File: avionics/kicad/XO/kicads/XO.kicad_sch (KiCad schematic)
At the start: 52 parts, among them SW1 SW_DIP_x02, X2Y-CAN 4.7nF_X2Y, X2Y-RS485 4.7nF_X2Y

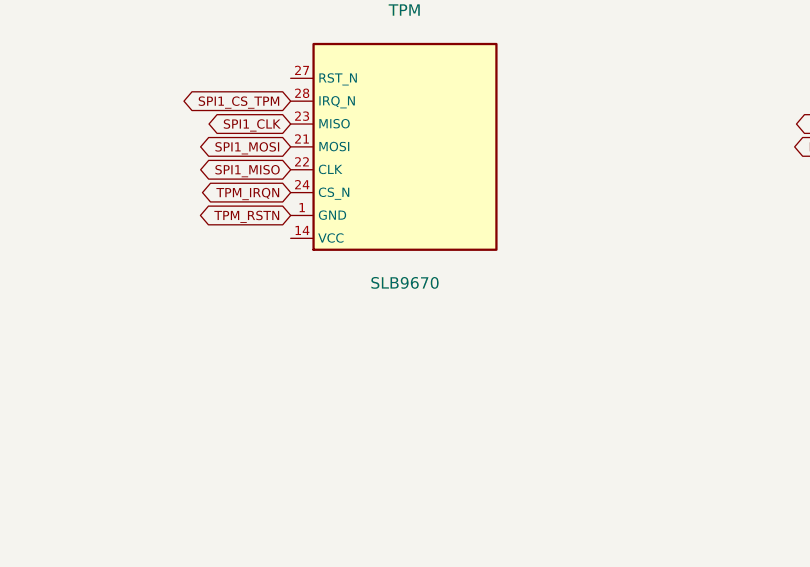
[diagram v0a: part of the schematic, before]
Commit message: Migrate fleet TPM from Infineon SLB9670 to SLB9672
Replaces every active reference to the SLB9670 TPM with SLB9672 across
KiCad symbols/schematics/PCBs/netlists, generator scripts, firmware
device-tree overlays, and documentation (REFERENCES.md, WBS/TODO,
current-specification, graphical build guide). Archived files, frozen
revision snapshots, and the old datasheet PDF are left untouched.

- Added avionics/datasheets/SLB_9672XU20_Infineon.pdf (Infineon DS Rev
  1.3, 2024-11-18) and a new clean-room symbol/pinmap
  (Observer_SLB9672_TPM.kicad_sym, SLB9672XU2_0_pinmap.csv), replacing
  the superseded SLB9670 symbol/pinmap.
- Verified the physical footprint is unchanged (5x5mm body, 0.5mm
  pitch, 32-pin QFN, 3.6x3.6mm exposed pad per both datasheets), so the
  existing Package_DFN_QFN:QFN-32-1EP_5x5mm_P0.5mm_EP3.45x3.45mm
  footprint was reused as-is. Pin *functions* do differ (SLB9672 makes
  pins 1/14/22 the mandatory VDD pins vs 8/22 on SLB9670; pin 6 is now a
  true no-connect instead of GPIO; pins 3/4/7 are GPIO_00/01/02 instead
  of NCI/NCI/PP) -- the new symbol and every net-map/pinmap that lists
  pin functions reflect the corrected pinout.
- Populated the corrected component into Observer, Commo, Flight
  Engineer, and CAN-PERIPH-GW-1's schematics (lib_symbol block +
  instances) and into every board's PCB Value/property text. Pilot's
  and XO's own independently-authored inline TPM symbols were text-
  renamed only, preserving their pre-existing (and separately tracked)
  wrong-pin-number defect -- out of scope for this swap.
- Firmware: infineon,slb9670 -> infineon,slb9672 compatible string and
  tpm_slb9670: -> tpm_slb9672: node label in both active cape DTS
  overlays.
- REFERENCES.md REF-SENSOR-011 updated in place with validated Infineon
  URLs; new open items logged for (a) re-running kicad-cli ERC/DRC
  (unavailable in this environment) and (b) a newly-found, unrelated
  pre-existing footprint-mismatch defect on XO's placed TPM.
- PROJECT_INDEX.md / t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
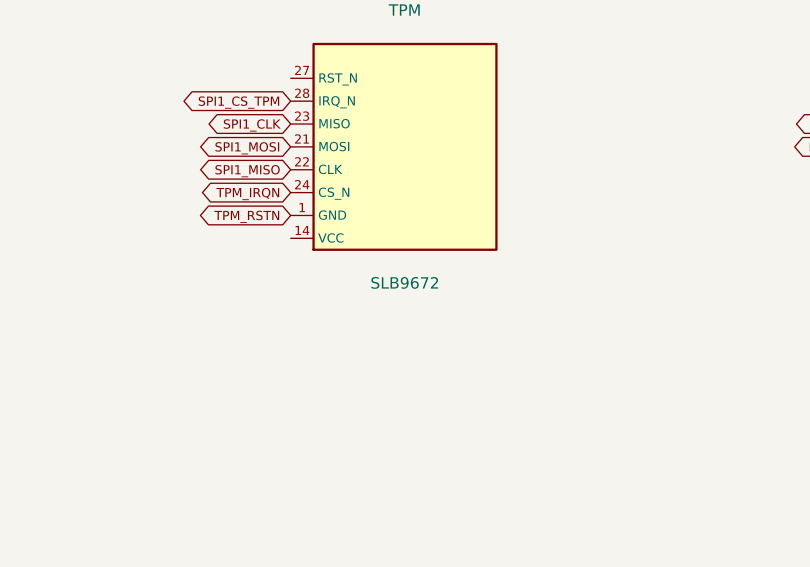
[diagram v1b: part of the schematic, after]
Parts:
- TPM: value SLB9670 -> SLB9672; symbol SLB9670 -> SLB9672
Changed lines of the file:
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@@
     (property "Intersheet References" "${INTERSHEET_REFS}" (at 292.70 352.54 0)
       (effects (font (size 1.016 1.016)) (hide yes))))
-  (symbol (lib_id "SLB9670") (at 210.00 350.00 0)
+  (symbol (lib_id "SLB9672") (at 210.00 350.00 0)
     (unit 1) (exclude_from_sim no) (in_bom yes) (on_board yes) (dnp no)
     (property "Reference" "TPM" (at 210.00 334.84 0) (effects (font (size 1.27 1.27))))
-    (property "Value" "SLB9670" (at 210.00 365.16 0) (effects (font (size 1.27 1.27))))
+    (property "Value" "SLB9672" (at 210.00 365.16 0) (effects (font (size 1.27 1.27))))
     (property "Footprint" "" (at 0 0 0) (effects (font (size 1.27 1.27)) (hide yes)))
     (property "Datasheet" "" (at 0 0 0) (effects (font (size 1.27 1.27)) (hide yes)))

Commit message: feat(avionics): XO schematic-first rebuild to ERC 0; PCB placement in progress
Replaces XO's legacy schematic/PCB (169 sch refs vs 43 PCB footprints, 564
ERC violations) with a fresh generator pipeline matching Pilot's method
(gen_xo_sch.py / gen_xo_footprints.py / gen_xo_pcb.py), all datasheet-verified.

Fleet-shared blocks reused verbatim from Pilot (same parts, same pin tables,
_B_-suffixed nets per XO.md's own documented bus-sharing rationale): ISOW1044
CAN-FD, ISOW1412 RS-485, HI-1573 + PM-DB2791S MIL-STD-1553B (retires the
DS26LV31/32 + fake "SM-1553-11" defect, same fix as Pilot), SLB9672 TPM,
DP83825I Ethernet PHY x1 (single PHY per WBS.md "XO: 1x PHY (RMII0)" —
resolves a 3-way doc contradiction over whether XO has Ethernet in favor of
WBS's more authoritative, more recent "restored at Rev R" entry).

New XO-unique blocks, each pin table transcribed from its own OEM datasheet:
RFD900x SiK UHF radio, RFM95W LoRa module, WL1837MOD WiFi+BT (~14 of 100
balls carry a net this pass, a disclosed scope calibration), TPS63031 RF
buck-boost rail, W25Q128JV SPI NOR flash, ATF16V8BQL used as a logging
write-block interlock (JEDEC fuse map is a firmware deliverable, out of
scope here), three antenna filter/ESD chains, microSD slot.

Two part-number defects found in XO.md's own antenna-filter BOM and
corrected (flagged, not silently fixed): Johanson "0915LP15B0100E" and
"2450BP15B050E" do not exist in Johanson's catalog (confirmed against their
product listings) — substituted with the closest real parts found
(0915LP15B026E, 2450BP15E0100); NEEDS owner confirmation. XO.md's cited
microSD connector "Molex 503182-1852" could not be verified real —
replaced with the confirmed-real Connector_Card:microSD_HC_Molex_104031-0811
already in KiCad's system library. RCLAMP0502B's datasheet PDF could not be
obtained from any source tried; its footprint is a reasonable SOD-882
estimate, not pixel-verified — flagged for a real datasheet fetch.

ERC 0 confirmed (kicad-cli sch erc --sev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
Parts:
- removed 1553-DRV: DS26LV31, symbol DS26LV31
- removed 1553-RCV: DS26LV32, symbol DS26LV32
- removed 1553-XFM: SM-1553-11, symbol SM-1553-11
- removed CAN-TR: ISOW1044BDFMR, Package_SO:SOIC-20W_7.5x12.8mm_P1.27mm, symbol ISOW1044BDFMR
- removed CMC-CAN, CMC-RS485, CM_ETH_B: SRF2012-100Y, Inductor_SMD:L_0805_2012Metric, symbol SRF2012
- removed D_1553: SMAJ33CA, Diode_SMD:D_SMA, symbol SMAJ33CA
- removed D_ANT_LORA, D_ANT_SIK, D_ANT_WIFI: RCLAMP0502B, Diode_SMD:D_SOD-882, symbol RCLAMP0502B
- removed D_CAN, D_RS485, D_XCVR_TVS, TVS_ETHB_RX, TVS_ETHB_TX: PRTR5V0U2X, Package_TO_SOT_SMD:SOT-363_SC-70-6, symbol PRTR5V0U2X
- removed ETH-PHY: DP83825I, Package_QFP:LQFP-32_7x7mm_P0.8mm, symbol DP83825I
- removed FB_PWR: 742792512, Inductor_SMD:L_0805_2012Metric, symbol Ferrite_Bead
- removed FL_LORA, FL_SIK: 0915LP15B0100E, Filter:BPF_1206, symbol BPF_915
- removed FL_WIFI: 2450BP15B050E, Filter:BPF_1206, symbol BPF_2400
- removed HX1188_B: HX1188NL, Package_SO:SOIC-16_3.9x9.9mm_P1.27mm, symbol HX1188NL
- removed J_1553: SM04B-GHS-TB-1MP — MIL-STD-1553B, Connector_JST:JST_GH_SM04B-GHS-TB_1x04-1MP_P1.25mm_Horizontal, symbol Conn_JST_GH_04P
- removed J_485: SM03B-GHS-TB-1MP — RS-485, Connector_JST:JST_GH_SM03B-GHS-TB_1x03-1MP_P1.25mm_Horizontal, symbol Conn_JST_GH_03P
- removed J_CAN: SM03B-GHS-TB-1MP — CAN FD, Connector_JST:JST_GH_SM03B-GHS-TB_1x03-1MP_P1.25mm_Horizontal, symbol Conn_JST_GH_03P
- removed J_ETH_B: SM06B-GHS-TB-1MP, Connector_JST:JST_GH_SM06B-GHS-TB_1x06-1MP_P1.25mm_Horizontal, symbol Conn_JST_GH_06P
- removed J_PWR: JST_GH_04P — Power Input, Connector_JST:JST_GH_SM04B-GHS-TB_1x04-1MP_P1.25mm_Horizontal, symbol Conn_JST_GH_04P
- removed J_SD: microSD, symbol MicroSD
- removed J_SIK_ANT: U.FL-R-SMT-1, Connector_Coaxial:U.FL_Hirose_UFL-R-SMT-1_Vertical, symbol Conn_UFL
- removed J_SMA_LORA, J_SMA_SIK, J_SMA_WIFI: Conn_SMA, Connector_Coaxial:SMA_Vertical_Straight, symbol Conn_SMA
- removed J_XCVR: Conn_JST_GH_06P, Connector_JST:JST_GH_SM06B-GHS-TB_1x06-1MP_P1.25mm_Horizontal, symbol Conn_JST_GH_06P
- removed LOAD-ADC: HX711, symbol HX711
- removed LORA: RFM95W, symbol RFM95W
- removed NOR-FLASH: W25Q128JV, symbol W25Q128JV
- removed PB2-P1: PB2I-P1-2x18, symbol Conn_36
- removed PB2-P2: PB2I-P2-2x18, symbol Conn_36
- removed PWM-I2C: PCA9685, symbol PCA9685
- removed RS485: ISOW1412, Package_SO:SOIC-20W_7.5x12.8mm_P1.27mm, symbol ISOW1412
- removed R_RBIAS_B: 49.9R_1%, Resistor_SMD:R_0402_1005Metric, symbol R_SMD
- removed R_SBUS_RX, R_XCVR_RX: 100R, Resistor_SMD:R_0402_1005Metric, symbol R_SMD
- removed SD-WB: ATF16V8BQL, symbol ATF16V8BQL
- removed SW1: SW_DIP_x02, Package_DIP:DIP-4_W7.62mm, symbol SW_DIP_x02
- removed TPM: SLB9672, symbol SLB9672
- removed U_ETH_B_1V8: TPS62933, Package_SO:SOIC-8_3.9x4.9mm_P1.27mm, symbol TPS62933
- removed U_SBUS_B: 74LVC1G14GW, Package_TO_SOT_SMD:SOT-23-5, symbol 74LVC1G14
- removed WIFI & BT: WL1837MOD, symbol WL1837MOD
- removed WINCH DRV: DRV8833, symbol DRV8833
- removed X2Y-CAN, X2Y-RS485: 4.7nF_X2Y, Capacitor_SMD:C_0402_1005Metric, symbol X2Y_4N7
- added 1553-XCVR: HI-1573PCI, Package_DFN_QFN:QFN-44-1EP_7x7mm_P0.5mm_EP5.2x5.2mm, symbol XO:S_1553-XCVR
- added 1553-XFM: PM-DB2791S, Serenity-Custom:Xfmr_1553_SMD_0.40in_8pin, symbol XO:S_1553-XFM
- added C-1553A: 100nF, Capacitor_SMD:C_0402_1005Metric, symbol XO:S_C-1553A
- added C-1553B: 100nF, Capacitor_SMD:C_0402_1005Metric, symbol XO:S_C-1553B
- added C-1553C: 10uF 6.3V X5R, Capacitor_SMD:C_0805_2012Metric, symbol XO:S_C-1553C
- added C-1V8-IN: 1uF, Capacitor_SMD:C_0402_1005Metric, symbol XO:S_C-1V8-IN
- added C-1V8-OUT: 1uF, Capacitor_SMD:C_0402_1005Metric, symbol XO:S_C-1V8-OUT
- added C-25M: 100nF, Capacitor_SMD:C_0402_1005Metric, symbol XO:S_C-25M
- added C-3V3-HF: 100nF, Capacitor_SMD:C_0402_1005Metric, symbol XO:S_C-3V3-HF
- added C-3V3-IN: 10uF 10V X5R, Capacitor_SMD:C_0805_2012Metric, symbol XO:S_C-3V3-IN
- added C-3V3-O1: 22uF 6.3V X5R, Capacitor_SMD:C_0805_2012Metric, symbol XO:S_C-3V3-O1
- added C-3V3-O2: 22uF 6.3V X5R, Capacitor_SMD:C_0805_2012Metric, symbol XO:S_C-3V3-O2
- added C-485-1: 10nF, Capacitor_SMD:C_0201_0603Metric, symbol XO:S_C-485-1
- added C-485-2: 10uF 10V X5R, Capacitor_SMD:C_0805_2012Metric, symbol XO:S_C-485-2
- added C-485-3: 100nF, Capacitor_SMD:C_0402_1005Metric, symbol XO:S_C-485-3
- added C-485-4: 10nF, Capacitor_SMD:C_0201_0603Metric, symbol XO:S_C-485-4
- added C-485-5: 10uF 10V X5R, Capacitor_SMD:C_0805_2012Metric, symbol XO:S_C-485-5
- added C-485-6: 100nF, Capacitor_SMD:C_0402_1005Metric, symbol XO:S_C-485-6
- added C-BS: 10nF 2kV, Capacitor_SMD:C_1808_4520Metric, symbol XO:S_C-BS
- added C-BST: 100nF, Capacitor_SMD:C_0402_1005Metric, symbol XO:S_C-BST
- added C-CAN1: 10nF, Capacitor_SMD:C_0201_0603Metric, symbol XO:S_C-CAN1
- added C-CAN2: 10uF 10V X5R, Capacitor_SMD:C_0805_2012Metric, symbol XO:S_C-CAN2
- added C-CAN3: 100nF, Capacitor_SMD:C_0402_1005Metric, symbol XO:S_C-CAN3
- added C-CAN4: 10nF, Capacitor_SMD:C_0201_0603Metric, symbol XO:S_C-CAN4
- added C-CAN5: 10uF 10V X5R, Capacitor_SMD:C_0805_2012Metric, symbol XO:S_C-CAN5
- added C-CAN6: 100nF, Capacitor_SMD:C_0402_1005Metric, symbol XO:S_C-CAN6
- added C-FLASH1: 100nF, Capacitor_SMD:C_0402_1005Metric, symbol XO:S_C-FLASH1
- added C-IN1: 47uF 10V X5R, Capacitor_SMD:C_1210_3225Metric, symbol XO:S_C-IN1
- added C-IN2: 10uF 10V X5R, Capacitor_SMD:C_0805_2012Metric, symbol XO:S_C-IN2
- added C-IN3: 100nF, Capacitor_SMD:C_0402_1005Metric, symbol XO:S_C-IN3
- added C-LORA1: 100nF, Capacitor_SMD:C_0402_1005Metric, symbol XO:S_C-LORA1
- added C-PHY-A1: 10nF, Capacitor_SMD:C_0201_0603Metric, symbol XO:S_C-PHY-A1
- added C-PHY-A2: 100nF, Capacitor_SMD:C_0402_1005Metric, symbol XO:S_C-PHY-A2
- added C-PHY-A3: 1uF, Capacitor_SMD:C_0402_1005Metric, symbol XO:S_C-PHY-A3
- added C-PHY-CRD1: 100nF, Capacitor_SMD:C_0402_1005Metric, symbol XO:S_C-PHY-CRD1
- added C-PHY-CRD2: 1uF, Capacitor_SMD:C_0402_1005Metric, symbol XO:S_C-PHY-CRD2
- added C-PHY-CTD1: 100nF, Capacitor_SMD:C_0402_1005Metric, symbol XO:S_C-PHY-CTD1
- added C-PHY-CTD2: 1uF, Capacitor_SMD:C_0402_1005Metric, symbol XO:S_C-PHY-CTD2
- added C-PLD1: 100nF, Capacitor_SMD:C_0402_1005Metric, symbol XO:S_C-PLD1
- added C-RF-IN1: 10uF 10V X5R, Capacitor_SMD:C_0805_2012Metric, symbol XO:S_C-RF-IN1
- added C-RF-IN2: 100nF, Capacitor_SMD:C_0402_1005Metric, symbol XO:S_C-RF-IN2
- added C-RF-O1: 22uF 6.3V X5R, Capacitor_SMD:C_0805_2012Metric, symbol XO:S_C-RF-O1
- added C-RF-O2: 22uF 6.3V X5R, Capacitor_SMD:C_0805_2012Metric, symbol XO:S_C-RF-O2
- added C-SIK1: 10uF 10V X5R, Capacitor_SMD:C_0805_2012Metric, symbol XO:S_C-SIK1
- added C-SIK2: 100nF, Capacitor_SMD:C_0402_1005Metric, symbol XO:S_C-SIK2
- added C-SS: 10nF, Capacitor_SMD:C_0201_0603Metric, symbol XO:S_C-SS
- added C-TPM1: 1uF, Capacitor_SMD:C_0402_1005Metric, symbol XO:S_C-TPM1
- added C-TPM2: 100nF, Capacitor_SMD:C_0402_1005Metric, symbol XO:S_C-TPM2
- added C-TPM3: 100nF, Capacitor_SMD:C_0402_1005Metric, symbol XO:S_C-TPM3
- added C-TPM4: 100nF, Capacitor_SMD:C_0402_1005Metric, symbol XO:S_C-TPM4
- added C-WIFI1: 100nF, Capacitor_SMD:C_0402_1005Metric, symbol XO:S_C-WIFI1
- added C-WIFI2: 10uF 6.3V X5R, Capacitor_SMD:C_0805_2012Metric, symbol XO:S_C-WIFI2
- added CAN-TR: ISOW1044BDFMR, Package_SO:SOIC-20W_7.5x12.8mm_P1.27mm, symbol XO:S_CAN-TR
- added CMC-CAN: SRF2012-100Y, Serenity-Custom:Bourns_SRF2012_4T, symbol XO:S_CMC-CAN
- added CMC-RS485: SRF2012-100Y, Serenity-Custom:Bourns_SRF2012_4T, symbol XO:S_CMC-RS485
- added D-ANT-LORA: RCLAMP0502B, Serenity-Custom:RCLAMP0502B_SOD882, symbol XO:S_D-ANT-LORA
- added D-ANT-SIK: RCLAMP0502B, Serenity-Custom:RCLAMP0502B_SOD882, symbol XO:S_D-ANT-SIK
- added D-ANT-WIFI: RCLAMP0502B, Serenity-Custom:RCLAMP0502B_SOD882, symbol XO:S_D-ANT-WIFI
- added ETH-PHY: DP83825IRHBR, Package_DFN_QFN:Texas_RMQ0024A_WQFN-24-1EP_3x3mm_P0.4mm_EP1.9x1.9mm, symbol XO:S_ETH-PHY
- added FB-SDIO1: 742792510, Inductor_SMD:L_0805_2012Metric, symbol XO:S_FB-SDIO1
- added FB-SDIO2: 742792510, Inductor_SMD:L_0805_2012Metric, symbol XO:S_FB-SDIO2
- added FB-SDIO3: 742792510, Inductor_SMD:L_0805_2012Metric, symbol XO:S_FB-SDIO3
- added FB-SDIO4: 742792510, Inductor_SMD:L_0805_2012Metric, symbol XO:S_FB-SDIO4
- added FB-SDIO5: 742792510, Inductor_SMD:L_0805_2012Metric, symbol XO:S_FB-SDIO5
- added FB-SDIO6: 742792510, Inductor_SMD:L_0805_2012Metric, symbol XO:S_FB-SDIO6
- added FB-SIK1: 742792510, Inductor_SMD:L_0805_2012Metric, symbol XO:S_FB-SIK1
- added FB-SIK2: 742792510, Inductor_SMD:L_0805_2012Metric, symbol XO:S_FB-SIK2
- added FB-SIK3: 742792510, Inductor_SMD:L_0805_2012Metric, symbol XO:S_FB-SIK3
- added FB-SIK4: 742792510, Inductor_SMD:L_0805_2012Metric, symbol XO:S_FB-SIK4
- added FB1: 742792510, Inductor_SMD:L_0805_2012Metric, symbol XO:S_FB1
- added FL-LORA: 0915LP15B026E, Serenity-Custom:Johanson_0915LP15B026E_SMD4, symbol XO:S_FL-LORA
- added FL-SIK: 0915LP15B026E, Serenity-Custom:Johanson_0915LP15B026E_SMD4, symbol XO:S_FL-SIK
- added FL-WIFI: 2450BP15E0100, Serenity-Custom:Johanson_2450BP15E0100_SMD4, symbol XO:S_FL-WIFI
- added H1: M2.5 PGND, Serenity-Custom:MountingHole_2.7mm_M2.5_PGND_Ring, symbol XO:S_H1
- added H2: M2.5 PGND, Serenity-Custom:MountingHole_2.7mm_M2.5_PGND_Ring, symbol XO:S_H2
- added H3: M2.5 PGND, Serenity-Custom:MountingHole_2.7mm_M2.5_PGND_Ring, symbol XO:S_H3
- added H4: M2.5 PGND, Serenity-Custom:MountingHole_2.7mm_M2.5_PGND_Ring, symbol XO:S_H4
- added J-1553: SM04B-GHS-TB, Connector_JST:JST_GH_SM04B-GHS-TB_1x04-1MP_P1.25mm_Horizontal, symbol XO:S_J-1553
- added J-485: SM03B-GHS-TB, Connector_JST:JST_GH_SM03B-GHS-TB_1x03-1MP_P1.25mm_Horizontal, symbol XO:S_J-485
- added J-CAN: SM03B-GHS-TB, Connector_JST:JST_GH_SM03B-GHS-TB_1x03-1MP_P1.25mm_Horizontal, symbol XO:S_J-CAN
- added J-ETH: SM04B-GHS-TB, Connector_JST:JST_GH_SM04B-GHS-TB_1x04-1MP_P1.25mm_Horizontal, symbol XO:S_J-ETH
- added J-FAN: SM03B-GHS-TB, Connector_JST:JST_GH_SM03B-GHS-TB_1x03-1MP_P1.25mm_Horizontal, symbol XO:S_J-FAN
- added J-SD: microSD push-pull, Connector_Card:microSD_HC_Molex_104031-0811, symbol XO:S_J-SD
- added J-SIK-ANT: U.FL-R-SMT-1, Connector_Coaxial:U.FL_Hirose_U.FL-R-SMT-1_Vertical, symbol XO:S_J-SIK-ANT
- added J-SMA-LORA: MMCX vertical, Connector_Coaxial:MMCX_Molex_73415-1471_Vertical, symbol XO:S_J-SMA-LORA
- added J-SMA-SIK: MMCX vertical, Connector_Coaxial:MMCX_Molex_73415-1471_Vertical, symbol XO:S_J-SMA-SIK
- added J-SMA-WIFI: MMCX vertical, Connector_Coaxial:MMCX_Molex_73415-1471_Vertical, symbol XO:S_J-SMA-WIFI
- added L-3V3: 3.3uH 2.25A, Serenity-Custom:L_WE-MAPI_3015, symbol XO:S_L-3V3
- added L-RF1: 2.2uH 3A, Inductor_SMD:L_0805_2012Metric, symbol XO:S_L-RF1
- added L-RF2: 2.2uH 3A, Inductor_SMD:L_0805_2012Metric, symbol XO:S_L-RF2
- added LORA: RFM95W, Serenity-Custom:HopeRF_RFM95W_Castellated_16, symbol XO:S_LORA
- added NOR-FLASH: W25Q128JVSIQ, Package_SO:SOIC-8_3.9x4.9mm_P1.27mm, symbol XO:S_NOR-FLASH
- added PB2-P1: PB2I-P1-2x18, Serenity-Custom:PocketBeagle2_2x18_P1_Socket, symbol XO:S_PB2-P1
- added PB2-P2: PB2I-P2-2x18, Serenity-Custom:PocketBeagle2_2x18_P2_Socket, symbol XO:S_PB2-P2
- added PWR-IN: Nano-Fit 4P, Serenity-Custom:Molex_NanoFit_1x04_Horizontal, symbol XO:S_PWR-IN
- added R-1553N: 55R 2%, Resistor_SMD:R_0603_1608Metric, symbol XO:S_R-1553N
- added R-1553P: 55R 2%, Resistor_SMD:R_0603_1608Metric, symbol XO:S_R-1553P
- added R-485T: 120R, Resistor_SMD:R_0603_1608Metric, symbol XO:S_R-485T
- added R-AD0: 2.49k, Resistor_SMD:R_0201_0603Metric, symbol XO:S_R-AD0
- added R-BSR: 75R, Resistor_SMD:R_0402_1005Metric, symbol XO:S_R-BSR
- added R-BST: 75R, Resistor_SMD:R_0402_1005Metric, symbol XO:S_R-BST
- added R-CANT: 120R, Resistor_SMD:R_0603_1608Metric, symbol XO:S_R-CANT
- added R-EN3: 100k, Resistor_SMD:R_0201_0603Metric, symbol XO:S_R-EN3
- added R-FB3H: 100k 1%, Resistor_SMD:R_0201_0603Metric, symbol XO:S_R-FB3H
- added R-FB3L: 32.4k 1%, Resistor_SMD:R_0201_0603Metric, symbol XO:S_R-FB3L
- added R-FLASH-WP: 10k, Resistor_SMD:R_0201_0603Metric, symbol XO:S_R-FLASH-WP
- added R-LORA-C: 33R, Resistor_SMD:R_0402_1005Metric, symbol XO:S_R-LORA-C
- added R-LORA-M1: 33R, Resistor_SMD:R_0402_1005Metric, symbol XO:S_R-LORA-M1
- added R-LORA-M2: 33R, Resistor_SMD:R_0402_1005Metric, symbol XO:S_R-LORA-M2
- added R-LORA-N: 33R, Resistor_SMD:R_0402_1005Metric, symbol XO:S_R-LORA-N
- added R-LORA-RST: 10k, Resistor_SMD:R_0201_0603Metric, symbol XO:S_R-LORA-RST
- added R-PGND: 0R, Resistor_SMD:R_0805_2012Metric, symbol XO:S_R-PGND
- added R-RBIAS: 6.49k 1%, Resistor_SMD:R_0201_0603Metric, symbol XO:S_R-RBIAS
- added R-TPM10: 10k, Resistor_SMD:R_0201_0603Metric, symbol XO:S_R-TPM10
- added R-TPMCS: 10k, Resistor_SMD:R_0201_0603Metric, symbol XO:S_R-TPMCS
- added R-WIFI-EN: 10k, Resistor_SMD:R_0201_0603Metric, symbol XO:S_R-WIFI-EN
- added RS485: ISOW1412DFMR, Package_SO:SOIC-20W_7.5x12.8mm_P1.27mm, symbol XO:S_RS485
- added SD-WB: ATF16V8BQL-15XI, Package_SO:TSSOP-20_4.4x6.5mm_P0.65mm, symbol XO:S_SD-WB
- added SIK: RFD900x, Serenity-Custom:RFDesign_RFD900x_2x8_THT, symbol XO:S_SIK
- added T-ETH: 749010012A, Serenity-Custom:Wurth_749010012A_WE-LAN, symbol XO:S_T-ETH
- added TPM: SLB9672XU20, Package_DFN_QFN:QFN-32-1EP_5x5mm_P0.5mm_EP3.6x3.6mm, symbol XO:S_TPM
- added TVS-1553N: SMAJ33CA, Diode_SMD:D_SMA, symbol XO:S_TVS-1553N
- added TVS-1553P: SMAJ33CA, Diode_SMD:D_SMA, symbol XO:S_TVS-1553P
- added TVS-CAN: PRTR5V0U2X, Package_TO_SOT_SMD:SOT-143, symbol XO:S_TVS-CAN
- added TVS-RS485: PRTR5V0U2X, Package_TO_SOT_SMD:SOT-143, symbol XO:S_TVS-RS485
- added U-1V8: TLV75718PDBVR, Package_TO_SOT_SMD:SOT-89-3, symbol XO:S_U-1V8
- added U-3V3: TPS62933DRLR, Package_TO_SOT_SMD:SOT-583-8, symbol XO:S_U-3V3
- added U-3V3RF: TPS63031DSKR, Serenity-Custom:TPS6303x_VSON-10_2p5, symbol XO:S_U-3V3RF
- added WIFI: WL1837MOD, Serenity-Custom:WL1837MOD_MOC_100, symbol XO:S_WIFI
- added X-25M: 25MHz 3.3V, Oscillator:Oscillator_SMD_ECS_2520MV-xxx-xx-4Pin_2.5x2.0mm, symbol XO:S_X-25M
- added X2Y-CAN: 4.7nF X2Y, Serenity-Custom:X2Y_0805_4T, symbol XO:S_X2Y-CAN
- added X2Y-RS485: 4.7nF X2Y, Serenity-Custom:X2Y_0805_4T, symbol XO:S_X2Y-RS485
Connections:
- net +3V3: now also 1553-XCVR.2 (RXENA), 1553-XCVR.24 (TXINHB), 1553-XCVR.38 (VDDA), 1553-XCVR.39 (VDDA), 1553-XCVR.6 (VDDB), 1553-XCVR.7 (VDDB), C-1553A.1 (P), C-1553B.1 (P), C-1553C.1 (P), C-1V8-IN.1 (P), C-25M.1 (P), C-3V3-O1.1 (P), C-3V3-O2.1 (P), C-485-3.1 (P), C-CAN3.1 (P), C-FLASH1.1 (P), C-PHY-A1.1 (P), C-PHY-A2.1 (P), C-PHY-A3.1 (P), C-PLD1.1 (P), C-TPM1.1 (P), C-TPM2.1 (P), C-TPM3.1 (P), C-TPM4.1 (P), CAN-TR.1 (VIO), ETH-PHY.19 (AVDD33_TX), ETH-PHY.23 (AVDD33_RX), J-SD.4 (VDD), L-3V3.2 (B), NOR-FLASH.7 (/HOLD_or_/RESET(IO3)), NOR-FLASH.8 (VCC), R-AD0.1 (A), R-FB3H.1 (A), R-FLASH-WP.1 (A), R-TPM10.1 (A), R-TPMCS.1 (A), RS485.1 (VIO), RS485.8 (EN/FLT), SD-WB.20 (VCC), TPM.1 (VDD)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
- net +5V: now also C-3V3-HF.1 (P), C-3V3-IN.1 (P), C-485-1.1 (P), C-485-2.1 (P), C-CAN1.1 (P), C-CAN2.1 (P), C-IN2.1 (P), C-IN3.1 (P), C-RF-IN1.1 (P), C-RF-IN2.1 (P), CAN-TR.9 (VDD), FB-SIK1.1 (IN), FB1.2 (OUT), J-FAN.2 (+5V), L-RF1.2 (B), PB2-P1.35 (P35), PB2-P2.35 (P35), R-EN3.1 (A), RS485.9 (VDD), U-3V3.3 (VIN), U-3V3RF.5 (VIN), U-3V3RF.8 (VINA)
- net +5V_IN: now also C-IN1.1 (P), FB1.1 (IN), PWR-IN.1 (+5V_IN), PWR-IN.2 (+5V_IN)
- net BUS_1553_B_N: now also J-1553.2 (BUS_N), R-1553N.2 (B), TVS-1553N.1 (A)
- net BUS_1553_B_P: now also J-1553.1 (BUS_P), R-1553P.2 (B), TVS-1553P.1 (A)
- net CAN_B_H: now also CAN-TR.19 (CANH), CMC-CAN.1 (W1_IN)
- net CAN_B_L: now also CAN-TR.18 (CANL), CMC-CAN.4 (W2_IN)
- net GND: now also 1553-XCVR.16 (RXENB), 1553-XCVR.17 (GNDB), 1553-XCVR.18 (GNDB), 1553-XCVR.19 (GNDB), 1553-XCVR.25 (TXB), 1553-XCVR.26 (TXB*), 1553-XCVR.3 (GNDA), 1553-XCVR.4 (GNDA), 1553-XCVR.45 (EP), 1553-XCVR.5 (GNDA), 1553-XFM.2 (PRI_CT), C-1553A.2 (N), C-1553B.2 (N), C-1553C.2 (N), C-1V8-IN.2 (N), C-1V8-OUT.2 (N), C-25M.2 (N), C-3V3-HF.2 (N), C-3V3-IN.2 (N), C-3V3-O1.2 (N), C-3V3-O2.2 (N), C-485-1.2 (N), C-485-2.2 (N), C-485-3.2 (N), C-CAN1.2 (N), C-CAN2.2 (N), C-CAN3.2 (N), C-FLASH1.2 (N), C-IN1.2 (N), C-IN2.2 (N), C-IN3.2 (N), C-LORA1.2 (N), C-PHY-A1.2 (N), C-PHY-A2.2 (N), C-PHY-A3.2 (N), C-PHY-CRD1.2 (N), C-PHY-CRD2.2 (N), C-PHY-CTD1.2 (N), C-PHY-CTD2.2 (N), C-PLD1.2 (N)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
- net LORA_DIO0: now also LORA.14 (DIO0), PB2-P2.27 (P27)
- net LORA_RESETN: now also LORA.6 (RESET), R-LORA-RST.2 (B)
- net PGND: now also C-BS.2 (N), D-ANT-LORA.2 (K), D-ANT-SIK.2 (K), D-ANT-WIFI.2 (K), H1.1 (PGND), H2.1 (PGND), H3.1 (PGND), H4.1 (PGND), J-1553.4 (SHIELD), J-1553.MP (SHIELD), J-485.MP (SHIELD), J-CAN.MP (SHIELD), J-ETH.MP (SHIELD), J-SMA-LORA.2 (SHIELD), J-SMA-SIK.2 (SHIELD), J-SMA-WIFI.2 (SHIELD), R-PGND.2 (B), TVS-1553N.2 (K), TVS-1553P.2 (K)
- net SDIO_CLK: now also FB-SDIO2.1 (IN), PB2-P2.19 (P19)
- net SDIO_CMD: now also FB-SDIO1.1 (IN), PB2-P2.20 (P20)
- net SDIO_D0: now also FB-SDIO3.1 (IN), PB2-P2.21 (P21)
- net SDIO_D1: now also FB-SDIO4.1 (IN), PB2-P2.22 (P22)
- net SDIO_D2: now also FB-SDIO5.1 (IN), PB2-P2.1 (P1)
- net SDIO_D3: now also FB-SDIO6.1 (IN), PB2-P2.2 (P2)
- net SD_CD: now also J-SD.11 (SW-NC), PB2-P1.17 (P17)
- net UART_SIK_RX: now also FB-SIK2.1 (IN), PB2-P1.31 (P31)
- net UART_SIK_TX: now also FB-SIK3.1 (IN), PB2-P1.32 (P32)
- new net +1V8_IO: C-1V8-OUT.1 (P), R-WIFI-EN.1 (A), U-1V8.2 (OUT), WIFI.38 (VIO)
- new net +3V3_PB2: PB2-P1.33 (P33), PB2-P1.34 (P34)
- new net +3V3_RF: C-LORA1.1 (P), C-RF-O1.1 (P), C-RF-O2.1 (P), C-WIFI1.1 (P), C-WIFI2.1 (P), L-RF2.2 (B), LORA.13 (3.3V), R-LORA-RST.1 (A), U-3V3RF.1 (VOUT), U-3V3RF.10 (FB), WIFI.46 (VBAT_IN), WIFI.47 (VBAT_IN)
- new net BST_3V3: C-BST.1 (P), U-3V3.6 (BST)
- new net CAN_B_H_F: CMC-CAN.2 (W1_OUT), J-CAN.1 (CAN_H), R-CANT.1 (A), TVS-CAN.1 (IO1)
- new net CAN_B_L_F: CMC-CAN.3 (W2_OUT), J-CAN.2 (CAN_L), R-CANT.2 (B), TVS-CAN.3 (IO2)
- new net CAN_B_STB: CAN-TR.4 (STB), PB2-P1.14 (P14)
- new net ETH-PHY_RBIAS: ETH-PHY.24 (RBIAS), R-RBIAS.1 (A)
- new net ETHB_BS: C-BS.1 (P), R-BSR.2 (B), R-BST.2 (B)
- new net ETHB_CRD: C-PHY-CRD1.1 (P), C-PHY-CRD2.1 (P), T-ETH.7 (CRD)
- new net ETHB_CTD: C-PHY-CTD1.1 (P), C-PHY-CTD2.1 (P), T-ETH.2 (CTD)
- new net ETHB_LINE_CRX: R-BSR.1 (A), T-ETH.10 (CRX)
- new net ETHB_LINE_CTX: R-BST.1 (A), T-ETH.15 (CTX)
- new net ETHB_LINE_RXN: J-ETH.4 (RXN), T-ETH.9 (RX-)
- new net ETHB_LINE_RXP: J-ETH.3 (RXP), T-ETH.11 (RX+)
- new net ETHB_LINE_TXN: J-ETH.2 (TXN), T-ETH.14 (TX-)
- new net ETHB_LINE_TXP: J-ETH.1 (TXP), T-ETH.16 (TX+)
- new net ETHB_RXN: ETH-PHY.22 (RXIN), T-ETH.8 (RD-)
- new net ETHB_RXP: ETH-PHY.21 (RXIP), T-ETH.6 (RD+)
- new net ETHB_TXN: ETH-PHY.18 (TXON), T-ETH.3 (TD-)
- new net ETHB_TXP: ETH-PHY.17 (TXOP), T-ETH.1 (TD+)
- new net FAN_PWM_B: J-FAN.3 (FAN_PWM), PB2-P2.5 (P5)
- new net FB_3V3: R-FB3H.2 (B), R-FB3L.1 (A), U-3V3.8 (FB)
- new net FLASH_WP_N: NOR-FLASH.3 (/WP(IO2)), R-FLASH-WP.2 (B), SD-WB.19 (I/O)
- new net GND2_CANB: C-CAN4.2 (N), C-CAN5.2 (N), C-CAN6.2 (N), CAN-TR.11 (GND2), CAN-TR.15 (GISOIN), CAN-TR.16 (GISOIN), CAN-TR.17 (GISOIN), J-CAN.3 (GND), TVS-CAN.2 (GND), X2Y-CAN.3 (G1), X2Y-CAN.4 (G2)
- new net GND2_RS485B: C-485-4.2 (N), C-485-5.2 (N), C-485-6.2 (N), J-485.3 (GND), RS485.11 (GND2), RS485.13 (MODE), RS485.15 (GISOIN), TVS-RS485.2 (GND), X2Y-RS485.3 (G1), X2Y-RS485.4 (G2)
- new net LORA_ANT_F: D-ANT-LORA.1 (A), FL-LORA.4 (OUT), J-SMA-LORA.1 (RF)
- new net LORA_ANT_RF: FL-LORA.1 (IN), LORA.9 (ANT)
- new net M1553B_N: 1553-XCVR.42 (BUSA*), 1553-XCVR.43 (BUSA*), 1553-XFM.3 (PRI_N)
- new net M1553B_P: 1553-XCVR.40 (BUSA), 1553-XCVR.41 (BUSA), 1553-XFM.1 (PRI_P)
- new net M1553B_SEC_N: 1553-XFM.8 (SEC_N), R-1553N.1 (A)
- new net M1553B_SEC_P: 1553-XFM.4 (SEC_P), R-1553P.1 (A)
- new net M1553B_TX_INH: 1553-XCVR.31 (TXINHA), PB2-P1.20 (P20)
- new net MCAN0_B_RX: CAN-TR.5 (RXD), PB2-P1.15 (P15)
- new net MCAN0_B_TX: CAN-TR.3 (TXD), PB2-P1.16 (P16)
- new net MDC0: ETH-PHY.14 (MDC), PB2-P2.18 (P18)
- new net MDIO0: ETH-PHY.13 (MDIO), PB2-P2.17 (P17)
- new net PHY1_INTRN: ETH-PHY.15 (INT_N), PB2-P2.16 (P16)
- new net PHY1_RSTN: ETH-PHY.12 (RESET_N), PB2-P2.15 (P15)
- new net PHY_XI_25M: ETH-PHY.8 (X1), X-25M.3 (OUT)
- new net PLD_CLK: PB2-P2.6 (P6), SD-WB.1 (I/CLK)
- new net PLD_I1: PB2-P2.7 (P7), SD-WB.2 (I1)
- new net PLD_I2: PB2-P2.8 (P8), SD-WB.3 (I2)
- new net PLD_I3: PB2-P2.13 (P13), SD-WB.4 (I3)
- new net PLD_I4: PB2-P2.14 (P14), SD-WB.5 (I4)
- new net PLD_I5: PB2-P2.23 (P23), SD-WB.6 (I5)
- new net PLD_I6: PB2-P2.24 (P24), SD-WB.7 (I6)
- new net PLD_I7: PB2-P2.25 (P25), SD-WB.8 (I7)
- new net PLD_I8: PB2-P2.26 (P26), SD-WB.9 (I8)
- new net PRU_1553B_RX_N: 1553-XCVR.29 (RXA*), PB2-P1.7 (P7)
- new net PRU_1553B_RX_P: 1553-XCVR.30 (RXA), PB2-P1.8 (P8)
- new net PRU_1553B_TX_N: 1553-XCVR.37 (TXA*), PB2-P1.9 (P9)
- new net PRU_1553B_TX_P: 1553-XCVR.36 (TXA), PB2-P1.10 (P10)
- new net RF_SW1: L-RF1.1 (A), U-3V3RF.4 (L1)
- new net RF_SW2: L-RF2.1 (A), U-3V3RF.2 (L2)
- new net RMII0_CRS_DV: ETH-PHY.4 (CRS_DV), PB2-P2.29 (P29)
- new net RMII0_RXD0: ETH-PHY.1 (RX_D0/PHYAD0), PB2-P2.31 (P31), R-AD0.2 (B)
- new net RMII0_RXD1: ETH-PHY.2 (RX_D1), PB2-P2.30 (P30)
- new net RMII0_RX_ER: ETH-PHY.3 (RX_ER), PB2-P2.28 (P28)
- new net RMII0_TXD0: ETH-PHY.6 (TX_D0), PB2-P2.34 (P34)
- new net RMII0_TXD1: ETH-PHY.7 (TX_D1), PB2-P2.33 (P33)
- new net RMII0_TX_EN: ETH-PHY.5 (TX_EN), PB2-P2.32 (P32)
- new net RS485_B_A: CMC-RS485.1 (W1_IN), RS485.17 (Y), RS485.20 (A)
- new net RS485_B_A_F: CMC-RS485.2 (W1_OUT), J-485.1 (A), R-485T.1 (A), TVS-RS485.1 (IO1)
- new net RS485_B_B: CMC-RS485.4 (W2_IN), RS485.18 (Z), RS485.19 (B)
- new net RS485_B_B_F: CMC-RS485.3 (W2_OUT), J-485.2 (B), R-485T.2 (B), TVS-RS485.3 (IO2)
- new net RS485_B_DE: PB2-P1.11 (P11), RS485.3 (DE), RS485.5 (RE)
- new net RS485_B_RX: PB2-P1.12 (P12), RS485.4 (R)
- new net RS485_B_TX: PB2-P1.13 (P13), RS485.2 (D)
- new net SDIO_CLK_F: FB-SDIO2.2 (OUT), WIFI.8 (WL_SDIO_CLK)
- new net SDIO_CMD_F: FB-SDIO1.2 (OUT), WIFI.6 (WL_SDIO_CMD)
- new net SDIO_D0_F: FB-SDIO3.2 (OUT), WIFI.10 (WL_SDIO_D0)
- new net SDIO_D1_F: FB-SDIO4.2 (OUT), WIFI.11 (WL_SDIO_D1)
- new net SDIO_D2_F: FB-SDIO5.2 (OUT), WIFI.12 (WL_SDIO_D2)
- new net SDIO_D3_F: FB-SDIO6.2 (OUT), WIFI.13 (WL_SDIO_D3)
- new net SIK_ANT_F: D-ANT-SIK.1 (A), FL-SIK.4 (OUT), J-SMA-SIK.1 (RF)
- new net SIK_ANT_RF: FL-SIK.1 (IN), J-SIK-ANT.1 (RF)
- new net SIK_CTS: FB-SIK4.1 (IN), PB2-P2.3 (P3)
- new net SIK_CTS_F: FB-SIK4.2 (OUT), SIK.3 (CTS)
- new net SIK_RTS: PB2-P2.4 (P4), SIK.11 (RTS)
- new net SIK_VCC_F: C-SIK1.1 (P), C-SIK2.1 (P), FB-SIK1.2 (OUT), SIK.4 (Vcc)
- new net SPI0_B_CLK: NOR-FLASH.6 (CLK), PB2-P1.25 (P25), R-LORA-C.1 (A), TPM.19 (SCLK)
- new net SPI0_B_CLK_F: LORA.4 (SCK), R-LORA-C.2 (B)
- new net SPI0_B_CS_FLASH: NOR-FLASH.1 (/CS), PB2-P1.22 (P22)
- new net SPI0_B_CS_LORA: PB2-P1.26 (P26), R-LORA-N.1 (A)
- new net SPI0_B_CS_LORA_F: LORA.5 (NSS), R-LORA-N.2 (B)
- new net SPI0_B_CS_TPM: PB2-P1.21 (P21), R-TPMCS.2 (B), TPM.20 (CS#)
- new net SPI0_B_MISO: NOR-FLASH.2 (DO(IO1)), PB2-P1.23 (P23), R-LORA-M1.1 (A), TPM.24 (MISO)
- new net SPI0_B_MISO_F: LORA.2 (MISO), R-LORA-M1.2 (B)
- new net SPI0_B_MOSI: NOR-FLASH.5 (DI(IO0)), PB2-P1.24 (P24), R-LORA-M2.1 (A), TPM.21 (MOSI)
- new net SPI0_B_MOSI_F: LORA.3 (MOSI), R-LORA-M2.2 (B)
- new net SS_3V3: C-SS.1 (P), U-3V3.7 (SS/PG)
- new net SW_3V3: C-BST.2 (N), L-3V3.1 (A), U-3V3.5 (SW)
- new net TPM_B_IRQN: PB2-P2.12 (P12), TPM.18 (PIRQ#)
- new net TPM_B_P10_PU: R-TPM10.2 (B), TPM.10 (NCI/VDD)
- new net TPM_B_RSTN: PB2-P2.11 (P11), TPM.17 (RST#)
- new net U3V3_EN: R-EN3.2 (B), U-3V3.2 (EN)
- new net UART_SIK_RX_F: FB-SIK2.2 (OUT), SIK.7 (RX)
- new net UART_SIK_TX_F: FB-SIK3.2 (OUT), SIK.9 (TX)
- new net VCC2_CANB: C-CAN4.1 (P), C-CAN5.1 (P), C-CAN6.1 (P), CAN-TR.12 (VISOOUT), CAN-TR.13 (VSIN), CAN-TR.20 (VISOIN), TVS-CAN.4 (VCC)
- new net VCC2_RS485B: C-485-4.1 (P), C-485-5.1 (P), C-485-6.1 (P), RS485.12 (VISOOUT), RS485.16 (VISOIN), TVS-RS485.4 (VCC)
- new net WIFI_ANT_F: D-ANT-WIFI.1 (A), FL-WIFI.4 (OUT), J-SMA-WIFI.1 (RF)
- new net WIFI_ANT_RF: FL-WIFI.1 (IN), WIFI.32 (RF_ANT1)
- new net WIFI_EN: PB2-P2.9 (P9), R-WIFI-EN.2 (B), WIFI.40 (WLAN_EN)
- new net WIFI_IRQ: PB2-P2.10 (P10), WIFI.14 (WLAN_IRQ)
- no-connect marks 25 -> 171
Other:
- note removed: "ETH_B sub-circuit: EMI-hardened 10/100BASE-TX Ethernet PHY — Rev R baseline DP83825I PHY + HX1188NL magnetics + TPS62933 1.8V SMPS + PRTR5V0U2X TVS + SRF2012 CMC JST SM06B-GHS-TB-1MP connector J_ETH_B — RMII0 to PocketBeagle 2 AM6254"
- note removed: "J_XCVR pin 4: XCVR serial RX (SW1-1) OR SBUS signal (SW1-2) Set SW1: pos 1 = XCVR-49MHz mode, pos 2 = SBUS RC mode"
- note removed: "LoRa 915 MHz: RFM95W ANT -> FL_LORA BPF(915) -> D_ANT_LORA ESD -> J_SMA_LORA"
- note removed: "SECTION 13 -- Antenna Filter Chains (EMI Hardening)"
- note removed: "SW1-1=XCVR, SW1-2=SBUS"
- note removed: "SiK 915 MHz: J_SIK_ANT U.FL -> FL_SIK BPF(915) -> D_ANT_SIK ESD -> J_SMA_SIK"
- note removed: "WiFi/BT 2.4 GHz: WL1837MOD ANT -> FL_WIFI BPF(2.4G) -> D_ANT_WIFI ESD -> J_SMA_WIFI"
- title: XO — EMI-Hardened Comms, Logging & Payload Cape -> XO — Comms / Logging / Payload Cape

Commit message: fix(avionics): XO passive footprint audit — fix 2 undersized parts, shrink 16
Per the owner's request to audit XO's passives for smaller-footprint
opportunities, checked every real package size against its OEM datasheet
before changing anything (same discipline as the rest of this rebuild) and
found the audit cut both ways:

Undersized — corrected upward, not shrunk:
- FB1 + FB-SIK1-4 + FB-SDIO1-6 (11 ferrite beads, MPN 742792510): the
  footprint was 0805, but Wurth's own datasheet SIZE/TYPE field says this
  part is 1812 (4.5x3.2mm) — a real land-vs-silicon mismatch, not a size
  preference. Corrected to Inductor_SMD:L_1812_4532Metric.
- L-RF1/L-RF2 (TPS63031 switching inductors): the MPN "744042002" could not
  be found as a real Wurth part anywhere and appears to have been fabricated
  during the XO rebuild. Corrected to Coilcraft LPS3015-222MRC, the vendor/
  series TPS63031's own datasheet (Table 3, Section 9.2.2.2) recommends;
  footprint changed to the body-size-matched Wurth MAPI-3015 land (flagged
  as not pixel-verified against Coilcraft's own drawing — no exact KiCad
  system footprint for this part exists).

Genuine shrinks (real smaller parts verified to exist):
- 10x "10uF 6.3-10V X5R" bulk caps 0805->0603 (C-IN2, C-3V3-IN, C-RF-IN1,
  C-CAN2, C-CAN5, C-485-2, C-485-5, C-1553C, C-SIK1, C-WIFI2).
- 4x "22uF 6.3V X5R" bulk caps 0805->0603 (C-3V3-O1/O2, C-RF-O1/O2).
- R-CANT/R-485T (120R bus termination, DNP by default) 0603->0402.

Not shrunk: R-1553P/R-1553N (55R 2% MIL-STD-1553B stub isolation resistors)
were flagged as possible 0603->0402 candidates but left alone pending a
pulse-power dissipation check, since they are standards-relevant. C-IN1
(47uF/10V, 1210) and C-BS (10nF/2kV Y2, 1808) are correctly sized already
(capacitance/voltage-driven, not a size preference).

Net effect: total footprint area rose slightly (3676 -> 3687 mm^2, still
~96% of the 3850 mm^2 two-sided theoretical ceiling) because the two
corrections outweighed the shrinks in are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
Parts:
- C-1553C, C-3V3-IN, C-3V3-O1, C-3V3-O2, C-485-2, C-485-5, C-CAN2, C-CAN5, C-IN2, C-RF-IN1, C-RF-O1, C-RF-O2, C-SIK1, C-WIFI2: footprint Capacitor_SMD:C_0805_2012Metric -> Capacitor_SMD:C_0603_1608Metric
- FB-SDIO1, FB-SDIO2, FB-SDIO3, FB-SDIO4, FB-SDIO5, FB-SDIO6, FB-SIK1, FB-SIK2, FB-SIK3, FB-SIK4, FB1: footprint Inductor_SMD:L_0805_2012Metric -> Inductor_SMD:L_1812_4532Metric
- L-RF1, L-RF2: footprint Inductor_SMD:L_0805_2012Metric -> Inductor_SMD:L_Wuerth_MAPI-3015; MPN 744042002 -> LPS3015-222MRC
- R-485T, R-CANT: footprint Resistor_SMD:R_0603_1608Metric -> Resistor_SMD:R_0402_1005Metric

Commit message: fix(avionics): XO SiK radio swapped RFD900x THT -> RFD900ux-SMT (fixes overhang)
The owner found the RFD900x (42.5x30mm THT module) overhangs the 55x35mm XO
cape in more than one direction, even mounted piggyback on standoffs. Swapped
to RF Design's own flush SMT variant, RFD900ux-SMT (21x29x4.2mm, ~48% of the
RFD900x's footprint area) — same manufacturer, same SiK-family lineage.

Real, verified from the datasheet the owner supplied ("RFD900ux DataSheet
v1.2.pdf"): §5.2/Fig 5-2 gives the full 28-pad pin layout (dual antenna
ANT1/ANT2, USB pins not yet implemented per the datasheet's own note, onboard
+3V3 LDO output, 4x spare GPIO, SWO debug, 3x spare digital I/O), and
§6.1/Fig 6-1/Table 6-1 gives the land pattern (2x14 castellated edge pads +
2 central GND/thermal pads). New footprint
Serenity-Custom/RFDesign_RFD900ux_SMT.kicad_mod — pad PITCH is estimated
(~1.9mm, back-calculated from body height and pad count) since the land
pattern figure's vector art wasn't machine-extractable at pad-to-pad
resolution; flagged for confirmation before a real fab order.

Only ANT1 is wired (single antenna, matching XO's one SMA/MMCX port per SiK
channel); ANT2, the USB pins, the onboard LDO output, and the spare GPIO/SWO/
P3.x pins are left NC — disclosed scope calibration, same pattern already
used for WL1837MOD's unused balls. J-SIK-ANT (the U.FL pigtail connector) is
REMOVED: it only existed because the old RFD900x THT module had no on-module
RF pad; RFD900ux-SMT's ANT1 is a direct PCB-trace coax launch pad, so
SIK_ANT_RF now runs straight from the module to FL-SIK on copper.

ERC 0 confirmed (131 parts, 700 pins).

IMPORTANT area trade-off: this fixes the physical overhang (a hard
mechanical blocker) but does NOT reduce XO's total footprint-area budget.
The previous RFD900x entry only budgeted its THT header footprint (piggyback
mount on standoffs, doesn't block the board surface underneath) at ~498 mm^2;
RFD900ux-SMT mounts FLUSH, so its full real body courtyard (~671 mm^2)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
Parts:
- removed J-1553: SM04B-GHS-TB, Connector_JST:JST_GH_SM04B-GHS-TB_1x04-1MP_P1.25mm_Horizontal, symbol XO:S_J-1553
- removed J-ETH: SM04B-GHS-TB, Connector_JST:JST_GH_SM04B-GHS-TB_1x04-1MP_P1.25mm_Horizontal, symbol XO:S_J-ETH
- removed J-SIK-ANT: U.FL-R-SMT-1, Connector_Coaxial:U.FL_Hirose_U.FL-R-SMT-1_Vertical, symbol XO:S_J-SIK-ANT
- removed R-1553N: 55R 2%, Resistor_SMD:R_0603_1608Metric, symbol XO:S_R-1553N
- removed TVS-1553N: SMAJ33CA, Diode_SMD:D_SMA, symbol XO:S_TVS-1553N
- removed TVS-1553P: SMAJ33CA, Diode_SMD:D_SMA, symbol XO:S_TVS-1553P
- added C-1553A: 100nF, Capacitor_SMD:C_0402_1005Metric, symbol XO:S_C-1553A
- added C-1553B: 100nF, Capacitor_SMD:C_0402_1005Metric, symbol XO:S_C-1553B
- added C-1553C: 10uF 6.3V X5R, Capacitor_SMD:C_0603_1608Metric, symbol XO:S_C-1553C
- added C-TPM1: 1uF, Capacitor_SMD:C_0402_1005Metric, symbol XO:S_C-TPM1
- added X-25M: 25MHz 3.3V, Oscillator:Oscillator_SMD_ECS_2520MV-xxx-xx-4Pin_2.5x2.0mm, symbol XO:S_X-25M
- J-1553: renamed from C-TPM1; value 1uF -> SM04B-GHS-TB; footprint Capacitor_SMD:C_0402_1005Metric -> Connector_JST:JST_GH_SM04B-GHS-TB_1x04-1MP_P1.25mm_Horizontal; symbol XO:S_C-TPM1 -> XO:S_J-1553; MPN (none) -> SM04B-GHS-TB(LF)(SN)
- J-ETH: renamed from X-25M; value 25MHz 3.3V -> SM04B-GHS-TB; footprint Oscillator:Oscillator_SMD_ECS_2520MV-xxx-xx-4Pin_2.5x2.0mm -> Connector_JST:JST_GH_SM04B-GHS-TB_1x04-1MP_P1.25mm_Horizontal; symbol XO:S_X-25M -> XO:S_J-ETH; MPN ECS-2520MV-250-BN-TR -> SM04B-GHS-TB(LF)(SN)
- R-1553N: renamed from C-1553A; value 100nF -> 55R 2%; footprint Capacitor_SMD:C_0402_1005Metric -> Resistor_SMD:R_0603_1608Metric; symbol XO:S_C-1553A -> XO:S_R-1553N
- SIK: value RFD900x -> RFD900ux-SMT; footprint Serenity-Custom:RFDesign_RFD900x_2x8_THT -> Serenity-Custom:RFDesign_RFD900ux_SMT; MPN RFD900X -> RFD900UX-SMT
- TVS-1553N: renamed from C-1553C; value 10uF 6.3V X5R -> SMAJ33CA; footprint Capacitor_SMD:C_0603_1608Metric -> Diode_SMD:D_SMA; symbol XO:S_C-1553C -> XO:S_TVS-1553N; MPN (none) -> SMAJ33CA
- TVS-1553P: renamed from C-1553B; value 100nF -> SMAJ33CA; footprint Capacitor_SMD:C_0402_1005Metric -> Diode_SMD:D_SMA; symbol XO:S_C-1553B -> XO:S_TVS-1553P; MPN (none) -> SMAJ33CA
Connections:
- net +3V3: now also C-1553A.1 (P), C-1553B.1 (P), C-1553C.1 (P), C-TPM1.1 (P), X-25M.4 (VDD); no longer J-1553.1 (P), J-ETH.4 (VDD), R-1553N.1 (P), TVS-1553N.1 (P), TVS-1553P.1 (P)
- net BUS_1553_B_N: now also J-1553.2 (BUS_N), R-1553N.2 (B), TVS-1553N.1 (A)
- net BUS_1553_B_P: now also J-1553.1 (BUS_P), TVS-1553P.1 (A)
- net ETHB_LINE_RXN: now also J-ETH.4 (RXN)
- net ETHB_LINE_RXP: now also J-ETH.3 (RXP)
- net ETHB_LINE_TXN: now also J-ETH.2 (TXN)
- net ETHB_LINE_TXP: now also J-ETH.1 (TXP)
- net GND: now also J-1553.3 (GND), SIK.11 (GND), SIK.12 (GND), SIK.14 (GND), SIK.15 (GND), SIK.17 (GND), SIK.18 (GND), SIK.20 (GND), SIK.29 (GND_THERMAL1), SIK.30 (GND_THERMAL2), SIK.8 (GND), SIK.9 (GND), C-1553A.2 (N), C-1553B.2 (N), C-1553C.2 (N), C-TPM1.2 (N), X-25M.2 (GND); no longer J-1553.2 (N), J-ETH.2 (GND), R-1553N.2 (N), SIK.1 (GND), SIK.16 (GND), SIK.2 (GND), TVS-1553N.2 (N), TVS-1553P.2 (N)
- net M1553B_SEC_N: now also R-1553N.1 (A)
- net PGND: now also J-1553.4 (SHIELD), J-1553.MP (SHIELD), J-ETH.MP (SHIELD), TVS-1553N.2 (K), TVS-1553P.2 (K)
- net PHY_XI_25M: now also X-25M.3 (OUT); no longer J-ETH.3 (OUT)
- net SIK_ANT_RF: now also SIK.13 (ANT1)
- net SIK_CTS_F: now also SIK.28 (CTS); no longer SIK.3 (CTS)
- net SIK_RTS: now also SIK.27 (RTS); no longer SIK.11 (RTS)
- net SIK_VCC_F: now also SIK.19 (+5V); no longer SIK.4 (Vcc)
- net UART_SIK_RX_F: now also SIK.25 (RX); no longer SIK.7 (RX)
- net UART_SIK_TX_F: now also SIK.26 (TX); no longer SIK.9 (TX)
- no-connect marks 171 -> 176
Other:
- moved on the sheet: R-1553N, TVS-1553N, TVS-1553P
